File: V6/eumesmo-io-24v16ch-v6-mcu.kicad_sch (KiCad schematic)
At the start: 19 parts, among them Q3 UMH3N, SW1 RESET, U3 TPS3820-33, U4 CH340K, U5 ESP32-WROOM-32UE-N16

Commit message: Renamed all files to eumesmo branding
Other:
- note added: "TEMPLATE FOR GPIO ASSIGNMENT {"NAME":"eumesmo-24V-16CH-V6","GPIO":[0,3200,0,3232,0,0,0,0,5536,10240,10241,0,0, 0,5600,0,0,0,0,5568,0,0,0,0,0,0,0,0,608,640,192,193,0,0,0,0],"FLAG":0,"BASE":1} See https://tasmota.github.io/docs/Templates/"
- note removed: "TEMPLATE FOR GPIO ASSIGNMENT {"NAME":"ESP-24V-16CH-V6","GPIO":[0,3200,0,3232,0,0,0,0,5536,10240,10241,0,0, 0,5600,0,0,0,0,5568,0,0,0,0,0,0,0,0,608,640,192,193,0,0,0,0],"FLAG":0,"BASE":1} See https://tasmota.github.io/docs/Templates/"
- title: ESP 24V 16xIn/16xOut/1-Wire Module -> eumesmo 24V 16xIn/16xOut/1-Wire Module
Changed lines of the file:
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@@
 	(paper "A4")
 	(title_block
-		(title "ESP 24V 16xIn/16xOut/1-Wire Module")
-		(date "2026-02-10")
-		(rev "V6.1")
+		(title "eumesmo 24V 16xIn/16xOut/1-Wire Module")
+		(date "2026-06-13")
+		(rev "V6.2")
 	)
 	(text "TASMOTA CONFIGS\nThe configs below must be applied via terminal/console and adjusted according to the\ndesired hostname, device name, network addresses and behavior of switches.\n\nConfigure switches:\n> backlog switchmode1 5; switchmode2 5; switchmode3 5; switchmode4 5; switchmode5 5;\n switchmode6 5; switchmode7 5; switchmode8 5; switchmode9 5; switchmode10 5;\n switchmode11 5; switchmode12 5; switchmode13 5; switchmode14 5; switchmode15 5;\n switchmode16 5\n\nConfigure device name:\n> devicename fararmio066022\n\nConfigure network:\n> backlog ethipaddress 10.112.66.22; ethsubnetmask 255.255.255.0; ethgateway 10.112.66.254;\n  wifi 0; hostname fararmio066022; topic fararmio066022; devicename fararmio066022"
@@
 		)
 	)
-	(text "TEMPLATE FOR GPIO ASSIGNMENT\n\n{\"NAME\":\"ESP-24V-16CH-V6\",\"GPIO\":[0,3200,0,3232,0,0,0,0,5536,10240,10241,0,0,\n0,5600,0,0,0,0,5568,0,0,0,0,0,0,0,0,608,640,192,193,0,0,0,0],\"FLAG\":0,\"BASE\":1}\n\nSee https://tasmota.github.io/docs/Templates/"
+	(text "TEMPLATE FOR GPIO ASSIGNMENT\n\n{\"NAME\":\"eumesmo-24V-16CH-V6\",\"GPIO\":[0,3200,0,3232,0,0,0,0,5536,10240,10241,0,0,\n0,5600,0,0,0,0,5568,0,0,0,0,0,0,0,0,608,640,192,193,0,0,0,0],\"FLAG\":0,\"BASE\":1}\n\nSee https://tasmota.github.io/docs/Templates/"
 		(exclude_from_sim no)
 		(at 15.24 133.35 0)
@@
 		)
 		(instances
-			(project "esp-24v-16ch-v6"
+			(project "eumesmo-io-24v16ch-v6"
 				(path "/2bc5a21a-1d79-419d-a592-6852cc07b00a/f2a42251-1da5-495a-abaf-29698c5bb0fe"
 					(reference "TP11")
@@
 		)
 		(instances
-			(project "esp-24v-16ch-v6"
+			(project "eumesmo-io-24v16ch-v6"
 				(path "/2bc5a21a-1d79-419d-a592-6852cc07b00a/f2a42251-1da5-495a-abaf-29698c5bb0fe"
 					(reference "#PWR046")
@@
 		)
 		(instances
-			(project "esp-24v-16ch-v6"
+			(project "eumesmo-io-24v16ch-v6"
 				(path "/2bc5a21a-1d79-419d-a592-6852cc07b00a/f2a42251-1da5-495a-abaf-29698c5bb0fe"
 					(reference "R18")
@@
 		)
 		(instances
-			(project "esp-24v-16ch-v6"
+			(project "eumesmo-io-24v16ch-v6"
 				(path "/2bc5a21a-1d79-419d-a592-6852cc07b00a/f2a42251-1da5-495a-abaf-29698c5bb0fe"
 					(reference "C17")
@@
 		)
 		(instances
-			(project "esp-24v-16ch-v6"
+			(project "eumesmo-io-24v16ch-v6"
 				(path "/2bc5a21a-1d79-419d-a592-6852cc07b00a/f2a42251-1da5-495a-abaf-29698c5bb0fe"
 					(reference "R13")
@@
 		)
 		(instances
-			(project "esp-24v-16ch-v6"
+			(project "eumesmo-io-24v16ch-v6"
 				(path "/2bc5a21a-1d79-419d-a592-6852cc07b00a/f2a42251-1da5-495a-abaf-29698c5bb0fe"
 					(reference "R14")
@@
 		)
 		(instances
-			(project "esp-24v-16ch-v6"
+			(project "eumesmo-io-24v16ch-v6"
 				(path "/2bc5a21a-1d79-419d-a592-6852cc07b00a/f2a42251-1da5-495a-abaf-29698c5bb0fe"
 					(reference "C18")
@@
 		)
 		(instances
-			(project "esp-24v-16ch-v6"
+			(project "eumesmo-io-24v16ch-v6"
 				(path "/2bc5a21a-1d79-419d-a592-6852cc07b00a/f2a42251-1da5-495a-abaf-29698c5bb0fe"
 					(reference "#PWR040")
@@
 		)
 		(instances
-			(project "esp-24v-16ch-v6"
+			(project "eumesmo-io-24v16ch-v6"
 				(path "/2bc5a21a-1d79-419d-a592-6852cc07b00a/f2a42251-1da5-495a-abaf-29698c5bb0fe"
 					(reference "#PWR036")
@@
 		)
 		(instances
-			(project "esp-24v-16ch-v6"
+			(project "eumesmo-io-24v16ch-v6"
 				(path "/2bc5a21a-1d79-419d-a592-6852cc07b00a/f2a42251-1da5-495a-abaf-29698c5bb0fe"
 					(reference "TP12")
@@
 		)
 		(instances
-			(project "esp-24v-16ch-v6"
+			(project "eumesmo-io-24v16ch-v6"
 				(path "/2bc5a21a-1d79-419d-a592-6852cc07b00a/f2a42251-1da5-495a-abaf-29698c5bb0fe"
 					(reference "Q3")
@@
 		)
 		(instances
-			(project "esp-24v-16ch-v6"
+			(project "eumesmo-io-24v16ch-v6"
 				(path "/2bc5a21a-1d79-419d-a592-6852cc07b00a/f2a42251-1da5-495a-abaf-29698c5bb0fe"
 					(reference "#PWR039")
@@
 		)
 		(instances
-			(project "esp-24v-16ch-v6"
+			(project "eumesmo-io-24v16ch-v6"
 				(path "/2bc5a21a-1d79-419d-a592-6852cc07b00a/f2a42251-1da5-495a-abaf-29698c5bb0fe"
 					(reference "Q3")
@@
 		)
 		(instances
-			(project "esp-24v-16ch-v6"
+			(project "eumesmo-io-24v16ch-v6"
 				(path "/2bc5a21a-1d79-419d-a592-6852cc07b00a/f2a42251-1da5-495a-abaf-29698c5bb0fe"
 					(reference "#PWR043")
@@
 		)
 		(instances
-			(project "esp-24v-16ch-v6"
+			(project "eumesmo-io-24v16ch-v6"
 				(path "/2bc5a21a-1d79-419d-a592-6852cc07b00a/f2a42251-1da5-495a-abaf-29698c5bb0fe"
 					(reference "R20")
@@
 		)
 		(instances
-			(project "esp-24v-16ch-v6"
+			(project "eumesmo-io-24v16ch-v6"
 				(path "/2bc5a21a-1d79-419d-a592-6852cc07b00a/f2a42251-1da5-495a-abaf-29698c5bb0fe"
 					(reference "SW1")
@@
 		)
 		(instances
-			(project "esp-24v-16ch-v6"
+			(project "eumesmo-io-24v16ch-v6"
 				(path "/2bc5a21a-1d79-419d-a592-6852cc07b00a/f2a42251-1da5-495a-abaf-29698c5bb0fe"
 					(reference "#PWR035")
@@
 		)
 		(instances
-			(project "esp-24v-16ch-v6"
+			(project "eumesmo-io-24v16ch-v6"
 				(path "/2bc5a21a-1d79-419d-a592-6852cc07b00a/f2a42251-1da5-495a-abaf-29698c5bb0fe"
 					(reference "C15")
@@
 		)
 		(instances
-			(project "esp-24v-16ch-v6"
+			(project "eumesmo-io-24v16ch-v6"
 				(path "/2bc5a21a-1d79-419d-a592-6852cc07b00a/f2a42251-1da5-495a-abaf-29698c5bb0fe"
 					(reference "#PWR031")
@@
 		)
 		(instances
-			(project "esp-24v-16ch-v6"
+			(project "eumesmo-io-24v16ch-v6"
 				(path "/2bc5a21a-1d79-419d-a592-6852cc07b00a/f2a42251-1da5-495a-abaf-29698c5bb0fe"
 					(reference "#PWR032")
@@
 		)
 		(instances
-			(project "esp-24v-16ch-v6"
+			(project "eumesmo-io-24v16ch-v6"
 				(path "/2bc5a21a-1d79-419d-a592-6852cc07b00a/f2a42251-1da5-495a-abaf-29698c5bb0fe"
 					(reference "#PWR042")
@@
 		)
 		(instances
-			(project "esp-24v-16ch-v6"
+			(project "eumesmo-io-24v16ch-v6"
 				(path "/2bc5a21a-1d79-419d-a592-6852cc07b00a/f2a42251-1da5-495a-abaf-29698c5bb0fe"
 					(reference "R17")
@@
 		)
 		(instances
-			(project "esp-24v-16ch-v6"
+			(project "eumesmo-io-24v16ch-v6"
 				(path "/2bc5a21a-1d79-419d-a592-6852cc07b00a/f2a42251-1da5-495a-abaf-29698c5bb0fe"
 					(reference "R19")
@@
 		)
 		(instances
-			(project "esp-24v-16ch-v6"
+			(project "eumesmo-io-24v16ch-v6"
 				(path "/2bc5a21a-1d79-419d-a592-6852cc07b00a/f2a42251-1da5-495a-abaf-29698c5bb0fe"
 					(reference "U5")
@@
 		)
 		(instances
-			(project "esp-24v-16ch-v6"
+			(project "eumesmo-io-24v16ch-v6"
 				(path "/2bc5a21a-1d79-419d-a592-6852cc07b00a/f2a42251-1da5-495a-abaf-29698c5bb0fe"
 					(reference "R16")
@@
 		)
 		(instances
-			(project "esp-24v-16ch-v6"
+			(project "eumesmo-io-24v16ch-v6"
 				(path "/2bc5a21a-1d79-419d-a592-6852cc07b00a/f2a42251-1da5-495a-abaf-29698c5bb0fe"
 					(reference "R15")
@@
 		)
 		(instances
-			(project "esp-24v-16ch-v6"
+			(project "eumesmo-io-24v16ch-v6"
 				(path "/2bc5a21a-1d79-419d-a592-6852cc07b00a/f2a42251-1da5-495a-abaf-29698c5bb0fe"
 					(reference "#PWR033")
@@
 		)
 		(instances
-			(project "esp-24v-16ch-v6"
+			(project "eumesmo-io-24v16ch-v6"
 				(path "/2bc5a21a-1d79-419d-a592-6852cc07b00a/f2a42251-1da5-495a-abaf-29698c5bb0fe"
 					(reference "#PWR044")
@@
 		)
 		(instances
-			(project "esp-24v-16ch-v6"
+			(project "eumesmo-io-24v16ch-v6"
 				(path "/2bc5a21a-1d79-419d-a592-6852cc07b00a/f2a42251-1da5-495a-abaf-29698c5bb0fe"
 					(reference "U3")
@@
 		)
 		(instances
-			(project "esp-24v-16ch-v6"
+			(project "eumesmo-io-24v16ch-v6"
 				(path "/2bc5a21a-1d79-419d-a592-6852cc07b00a/f2a42251-1da5-495a-abaf-29698c5bb0fe"
 					(reference "#PWR038")
@@
 		)
 		(instances
-			(project "esp-24v-16ch-v6"
+			(project "eumesmo-io-24v16ch-v6"
 				(path "/2bc5a21a-1d79-419d-a592-6852cc07b00a/f2a42251-1da5-495a-abaf-29698c5bb0fe"
 					(reference "#PWR037")
@@
 		)
 		(instances
-			(project "esp-24v-16ch-v6"
+			(project "eumesmo-io-24v16ch-v6"
 				(path "/2bc5a21a-1d79-419d-a592-6852cc07b00a/f2a42251-1da5-495a-abaf-29698c5bb0fe"
 					(reference "#PWR041")
@@
 		)
 		(instances
-			(project "esp-24v-16ch-v6"
+			(project "eumesmo-io-24v16ch-v6"
 				(path "/2bc5a21a-1d79-419d-a592-6852cc07b00a/f2a42251-1da5-495a-abaf-29698c5bb0fe"
 					(reference "#PWR047")
@@
 		)
 		(instances
-			(project "esp-24v-16ch-v6"
+			(project "eumesmo-io-24v16ch-v6"
 				(path "/2bc5a21a-1d79-419d-a592-6852cc07b00a/f2a42251-1da5-495a-abaf-29698c5bb0fe"
 					(reference "U4")
@@
 		)
 		(instances
-			(project "esp-24v-16ch-v6"
+			(project "eumesmo-io-24v16ch-v6"
 				(path "/2bc5a21a-1d79-419d-a592-6852cc07b00a/f2a42251-1da5-495a-abaf-29698c5bb0fe"
 					(reference "C16")
@@
 		)
 		(instances
-			(project "esp-24v-16ch-v6"
+			(project "eumesmo-io-24v16ch-v6"
 				(path "/2bc5a21a-1d79-419d-a592-6852cc07b00a/f2a42251-1da5-495a-abaf-29698c5bb0fe"
 					(reference "#PWR034")
@@
 		)
 		(instances
-			(project "esp-24v-16ch-v6"
+			(project "eumesmo-io-24v16ch-v6"
 				(path "/2bc5a21a-1d79-419d-a592-6852cc07b00a/f2a42251-1da5-495a-abaf-29698c5bb0fe"
 					(reference "#PWR045")

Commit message: Update eumesmo-io-24v16ch-v6-mcu.kicad_sch
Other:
- note added: "TEMPLATE FOR GPIO ASSIGNMENT {"NAME":"eumesmo-io-24v16ch-v6","GPIO":[0,3200,0,3232,0,0,0,0,5536,10240,10241,0,0, 0,5600,0,0,0,0,5568,0,0,0,0,0,0,0,0,608,640,192,193,0,0,0,0],"FLAG":0,"BASE":1} See https://tasmota.github.io/docs/Templates/"
- note removed: "TEMPLATE FOR GPIO ASSIGNMENT {"NAME":"eumesmo-24V-16CH-V6","GPIO":[0,3200,0,3232,0,0,0,0,5536,10240,10241,0,0, 0,5600,0,0,0,0,5568,0,0,0,0,0,0,0,0,608,640,192,193,0,0,0,0],"FLAG":0,"BASE":1} See https://tasmota.github.io/docs/Templates/"
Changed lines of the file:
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@@
 		)
 	)
-	(text "TEMPLATE FOR GPIO ASSIGNMENT\n\n{\"NAME\":\"eumesmo-24V-16CH-V6\",\"GPIO\":[0,3200,0,3232,0,0,0,0,5536,10240,10241,0,0,\n0,5600,0,0,0,0,5568,0,0,0,0,0,0,0,0,608,640,192,193,0,0,0,0],\"FLAG\":0,\"BASE\":1}\n\nSee https://tasmota.github.io/docs/Templates/"
+	(text "TEMPLATE FOR GPIO ASSIGNMENT\n\n{\"NAME\":\"eumesmo-io-24v16ch-v6\",\"GPIO\":[0,3200,0,3232,0,0,0,0,5536,10240,10241,0,0,\n0,5600,0,0,0,0,5568,0,0,0,0,0,0,0,0,608,640,192,193,0,0,0,0],\"FLAG\":0,\"BASE\":1}\n\nSee https://tasmota.github.io/docs/Templates/"
 		(exclude_from_sim no)
 		(at 15.24 133.35 0)

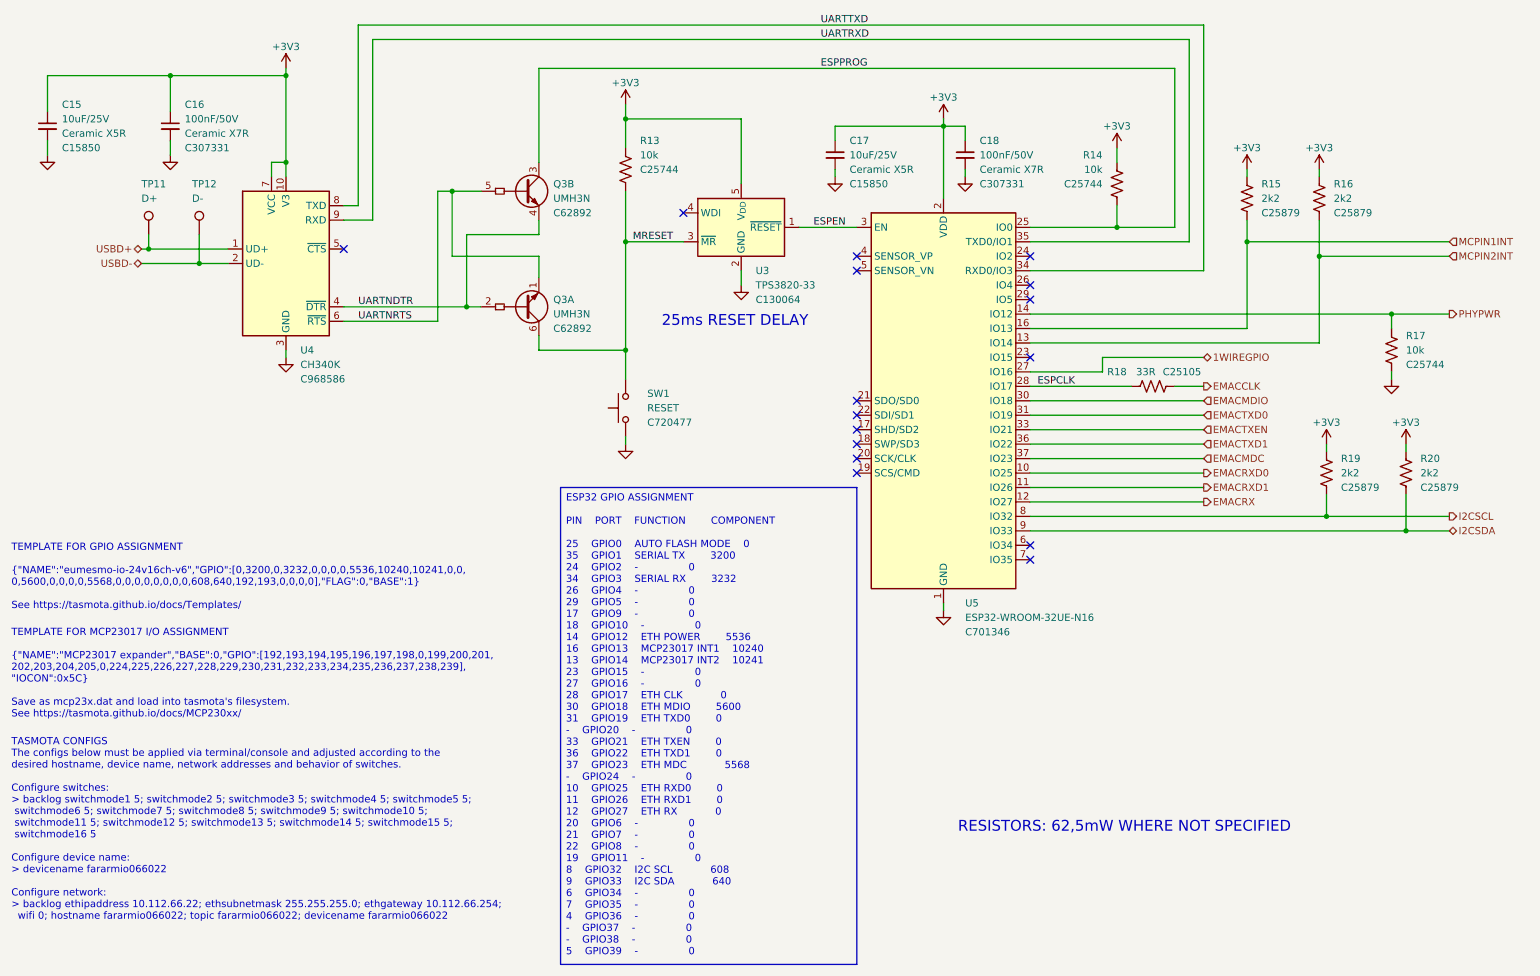
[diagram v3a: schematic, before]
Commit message: Added CPU health LED
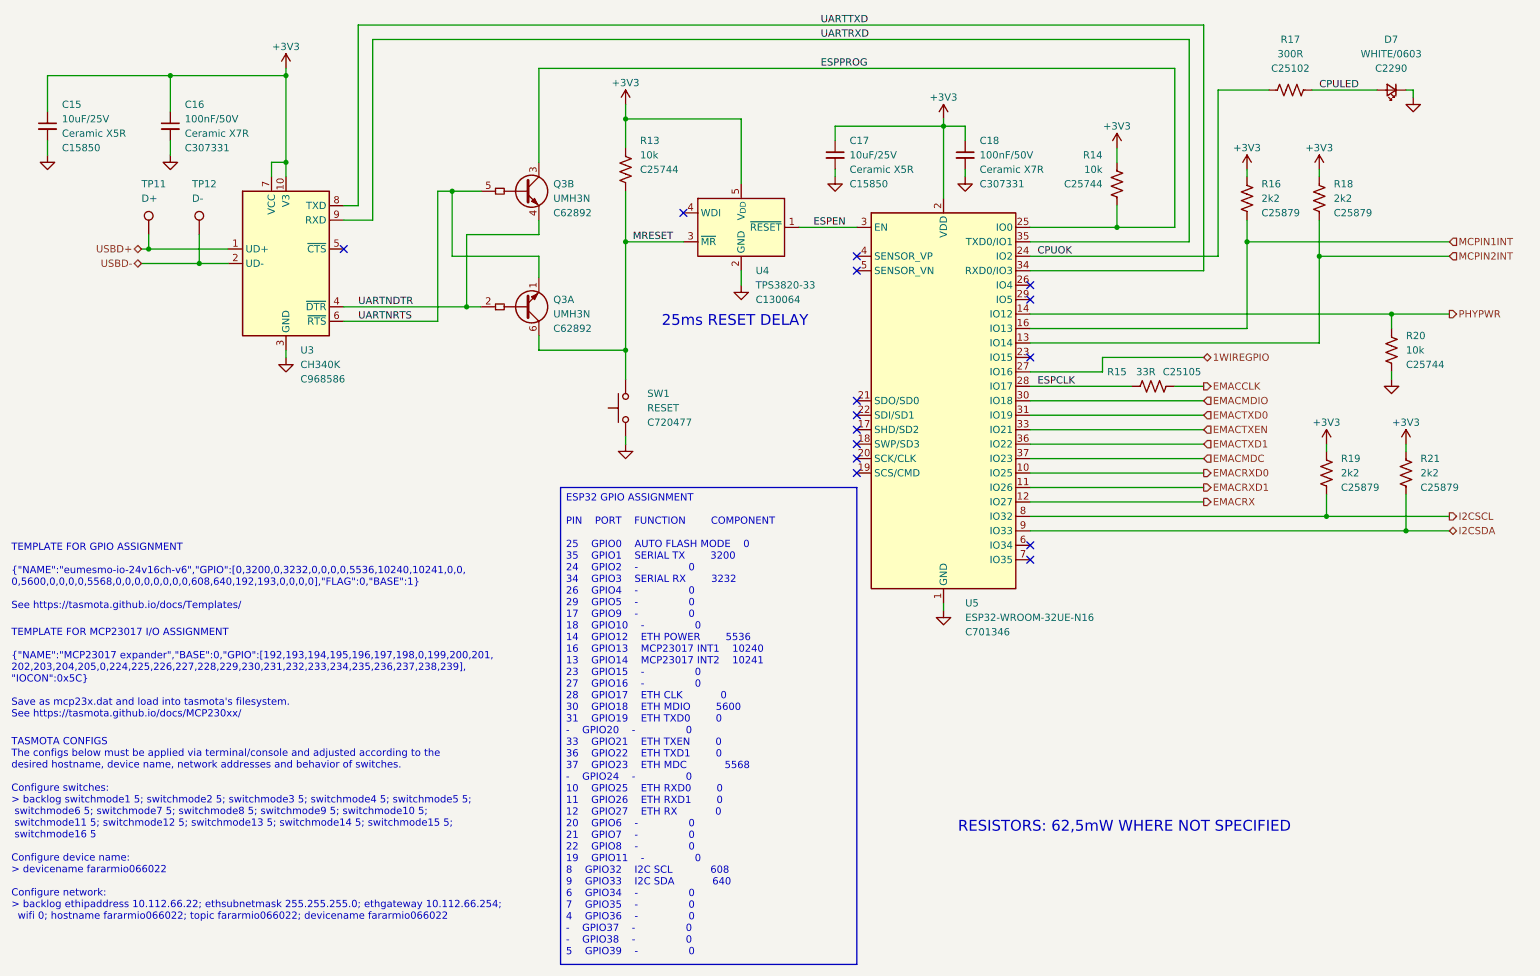
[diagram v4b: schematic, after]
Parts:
- added D7: WHITE/0603, Tales:LED_0603_1608Metric, symbol Device:LED_Small
- added R17: 300R, Tales:R_0402_1005Metric, symbol Device:R_US
- renumbered R18 to R15, R15 to R16, R16 to R18, R17 to R20, R20 to R21, U4 to U3, U3 to U4
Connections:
- net GND: now also D7.1 (K)
- net CPUOK: now reaches U5.24 (IO2)
- net CPUOK: now also R17.1
- new net CPULED: D7.2 (A), R17.2
- no-connect marks 16 -> 15
